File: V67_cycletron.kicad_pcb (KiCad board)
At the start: 4 copper layers, 101.9 x 49.8 mm, 33 parts, among them J1 USB_C_Receptacle_USB2.0_16P, J3 Screw_Terminal_01x11, U1 LM1117DT-5.0, U2 LM1117DT-3.3, U4 ESP32-S3-WROOM-1

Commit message: progress so far, believe I just need to ensure manufacture compatibility
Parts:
- removed vdo1: 5023520200, Connector_4:CONN_SD-502352-001_02_MOL
- added D1: D_Schottky, Diode_SMD:D_SMA, F.Cu at (79.8, 107.2)
- added Fan1: PC_Fan, connector_4_vert:CONN4_B4B-PH_JST, F.Cu at (137.5, 113.4)
- added HBridge1: B6B-PH-K-S, connector_6_vert:CONN_B6B-PH-K-S_JST, F.Cu at (101.5, 113.4)
- added HBridge2: B2B-PH-K-S, connector_2_vert:CONN2_B2B-PH-K-S_JST, F.Cu at (119.3, 113.4)
- added Hall1: Hall_Sens, connector_3_vert:CONN_B3B-PH-K-SLFSN_JST, F.Cu at (126.8, 113.4)
- added I2C1: MCP9600, connector_4_vert:CONN4_B4B-PH_JST, F.Cu at (145.1, 107.9)
- added J2: Conn_01x04_Socket, Connector_PinHeader_1.27mm:PinHeader_1x04_P1.27mm_Vertical, F.Cu at (146.1, 93.3)
- added Mos1: B2B-PH-K-S, connector_2_vert:CONN2_B2B-PH-K-S_JST, F.Cu at (80.0, 114.3)
- added R3: 1k, Resistor_SMD:R_0805_2012Metric_Pad1.20x1.40mm_HandSolder, F.Cu at (107.7, 96.5)
- added R4: 4.7k, Resistor_SMD:R_0805_2012Metric_Pad1.20x1.40mm_HandSolder, F.Cu at (141.7, 107.2)
- added R5: 4.7k, Resistor_SMD:R_0805_2012Metric_Pad1.20x1.40mm_HandSolder, F.Cu at (141.7, 100.1)
- added Therm1: B2B-PH-K-S, connector_2_vert:CONN2_B2B-PH-K-S_JST, F.Cu at (92.1, 113.4)
- added mosfet4: HD2305, Package_TO_SOT_SMD:SOT-23, F.Cu at (84.8, 108.3)
- added tr3: 1k, Resistor_SMD:R_0805_2012Metric_Pad1.20x1.40mm_HandSolder, F.Cu at (85.4, 103.6)
- Input1: renamed from input1; value 5023520200 -> B2B-PH-K-S; footprint Connector_4:CONN_SD-502352-001_02_MOL -> connector_2_vert:CONN2_B2B-PH-K-S_JST
- J3: value Screw_Terminal_01x11 -> Conn_01x04_Socket; footprint TerminalBlock:TerminalBlock_MaiXu_MX126-5.0-11P_1x11_P5.00mm -> Connector_PinHeader_1.27mm:PinHeader_1x04_P1.27mm_Vertical
- Motor1: value 5023520400 -> Motor1; footprint Connector_4:CONN_SD-502352-001_04_MOL -> connector_4_vert:CONN4_B4B-PH_JST
- Motor2: value 5023520400 -> Motor2; footprint Connector_4:CONN_SD-502352-001_04_MOL -> connector_4_vert:CONN4_B4B-PH_JST
- moved Rails1 41.2 mm to (43.6, 76.8)
- moved C2 34.6 mm to (141.6, 81.0)
- moved C1 33.8 mm to (143.8, 81.0)
- moved R_En1 30.5 mm to (140.2, 85.0), turned to 90 degrees
- moved Boot1 29.6 mm to (144.8, 88.8)
- moved En1 29.6 mm to (144.8, 85.0), turned to 0 degrees
- moved J3 25.7 mm to (142.2, 93.2), turned to 0 degrees
- moved R_boot1 25.0 mm to (140.0, 89.2), turned to -90 degrees
- moved vd_c2 13.4 mm to (90.2, 107.3), turned to 180 degrees
- moved vd_c1 11.9 mm to (92.1, 104.1)
- moved Motor1 8.89 mm to (42.4, 113.2), turned to 90 degrees
- moved Motor2 6.64 mm to (42.4, 93.5), turned to 90 degrees
- moved Motor_1 5.30 mm to (73.9, 101.9)
- moved Motor_2 5.30 mm to (73.9, 85.6)
- moved vd_r1 4.97 mm to (97.2, 105.4), turned to 90 degrees
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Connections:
- J3 pad 1: I20 -> IO40
- J3 pad 2: I19 -> IO39
- J3 pad 3: I18 -> IO38
- J3 pad 4: I17 -> IO37
- Motor1 pad 1: Motor1_A1 -> Motor1_A2
- Motor1 pad 2: Motor1_A2 -> Motor1_A1
- Motor1 pad 3: Motor1_B2 -> Motor1_B1
- Motor1 pad 4: Motor1_B1 -> Motor1_B2
- Motor2 pad 3: Motor2_B2 -> Motor2_B1
- Motor2 pad 4: Motor2_B1 -> Motor2_B2
- U4 pad 10: I10 -> Motor2_DIR
- U4 pad 11: I11 -> Motor1_FLT
- U4 pad 12: I12 -> Motor1_EN
- U4 pad 15: I15 -> Motor1_M0
- U4 pad 16: I16 -> Motor1_M1
- U4 pad 17: I17 -> Motor1_M2
- U4 pad 18: I18 -> Motor1_STEP
- U4 pad 19: I19 -> Motor1_DIR
- U4 pad 20: I20 -> mosfet1_i
- U4 pad 22: mosfet1_i -> L_EN
- U4 pad 23: mosfet2_i -> R_EN
- U4 pad 24: mosfet3_i -> LPWM
- U4 pad 25: Motor1_FLT -> RPWM
- U4 pad 26: Motor1_EN -> Hall_i
- U4 pad 28: Motor1_M0 -> FAN_En_o
- U4 pad 29: Motor1_M1 -> FAN_Tach_i
- U4 pad 30: Motor1_M2 -> IO37
- U4 pad 31: Motor1_STEP -> IO38
- U4 pad 32: Motor1_DIR -> IO39
- U4 pad 33: Motor2_EN -> IO40
- U4 pad 34: Motor2_FLT -> SCL
- U4 pad 35: Motor2_M0 -> SDA
- U4 pad 36: Motor2_M1 -> RX
- U4 pad 37: Motor2_M2 -> TX
- U4 pad 38: Motor2_STEP -> IO2
- U4 pad 39: Motor2_DIR -> IO1
- U4 pad 4: IO4 -> Motor2_FLT
- U4 pad 5: IO5 -> Motor2_EN
- U4 pad 6: IO6 -> Motor2_M0
- U4 pad 7: IO7 -> Motor2_M1
- U4 pad 8: I08 -> Motor2_M2
- U4 pad 9: I09 -> Motor2_STEP
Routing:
- net Motor1_EN: track 0.00 -> 72.0 mm, vias 0 -> 1
- net Motor1_M0: track 0.00 -> 70.7 mm, vias 0 -> 1
- net Motor2_EN: track 0.00 -> 70.2 mm, vias 0 -> 1
- net Motor1_M1: track 0.00 -> 68.6 mm, vias 0 -> 1
- net Motor2_M0: track 0.00 -> 67.6 mm, vias 0 -> 1
- net Motor1_M2: track 0.00 -> 67.1 mm, vias 0 -> 1
- net Motor2_M1: track 0.00 -> 64.4 mm, vias 0 -> 1
- net Motor1_STEP: track 0.00 -> 61.7 mm, vias 0 -> 1
- net Motor2_M2: track 0.00 -> 59.8 mm, vias 0 -> 1
- net Motor1_DIR: track 0.00 -> 59.5 mm, vias 0 -> 1
- net Motor2_STEP: track 0.00 -> 52.7 mm, vias 0 -> 1
- net Motor1_FLT: track 0.00 -> 52.1 mm, vias 0 -> 1
- net Motor2_DIR: track 0.00 -> 49.5 mm, vias 0 -> 1
- net Motor2_FLT: track 0.00 -> 49.1 mm, vias 0 -> 1
- net mosfet1_i: track 0.00 -> 44.4 mm
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- added copper zone on F.Cu, net +12V
- added copper zone on In1.Cu, net 3V3
- added copper zone on In2.Cu, net GND
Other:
- board size 101.9 x 49.8 mm -> 107.8 x 44.1 mm
- board text added: "0.01uF"
- board text added: "100"
- board text added: "100nF"
- board text added: "100uF"
- board text added: "10uF"
- board text added: "1k"
- board text added: "1uF"
- board text added: "2.2uF"
- board text added: "22uF"
- board text added: "3v3"
- board text added: "4.7k"
- board text added: "5.1k"
- board text added: "A1"
- board text added: "A2"
- board text added: "B1"
- board text added: "B2"
- board text added: "EN"
- board text added: "GND"
- board text added: "Hall"
- board text added: "In"
- board text added: "Input"
- board text added: "LEN"
- board text added: "LP"
- board text added: "REN"
- board text added: "RP"
- board text added: "SCL"
- board text added: "SDA"
- board text added: "Tach"

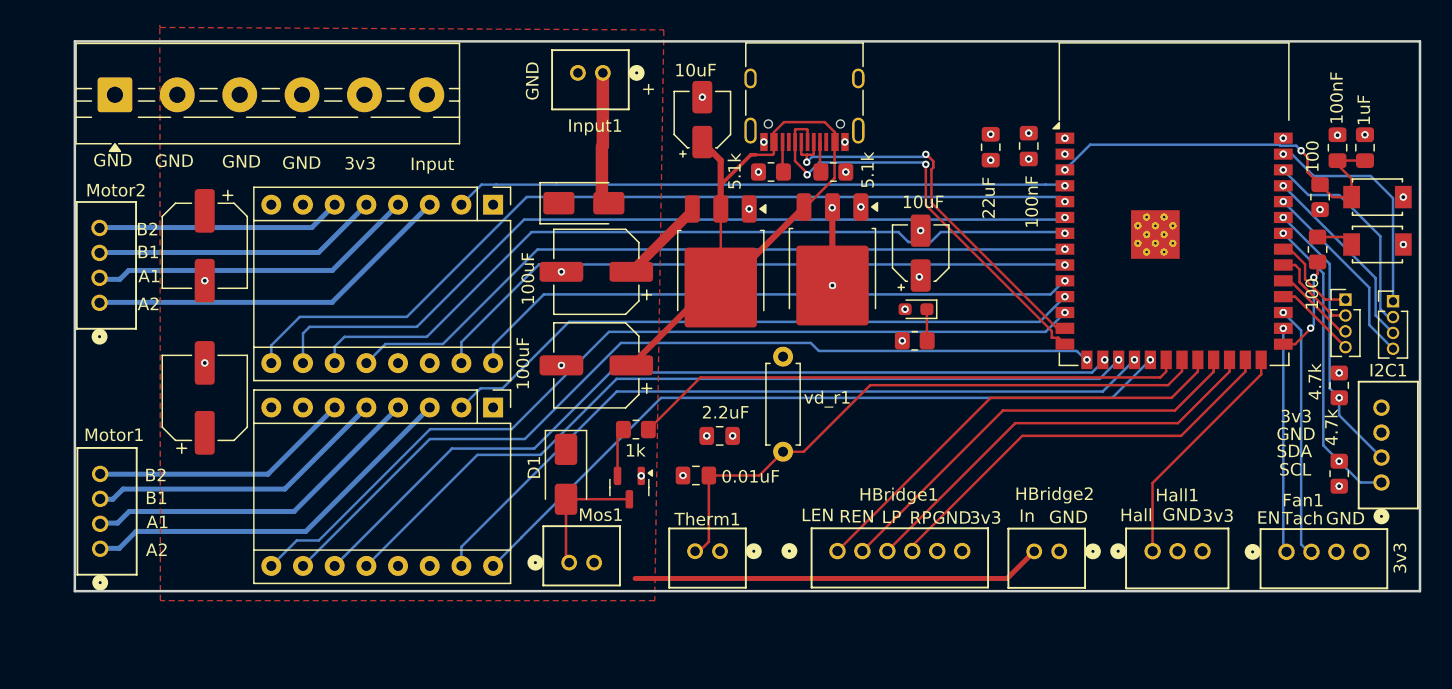
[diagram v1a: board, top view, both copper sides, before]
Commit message: re-arranged connector positions
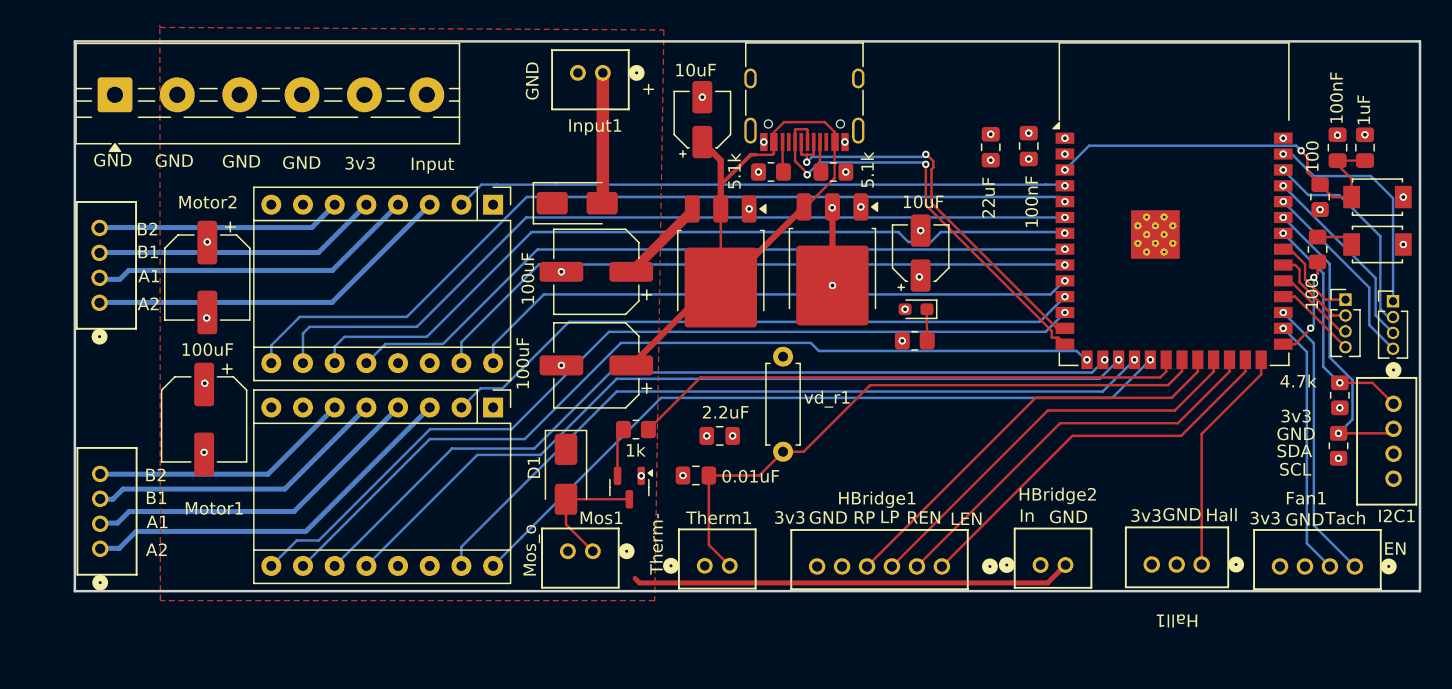
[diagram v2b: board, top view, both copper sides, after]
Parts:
- moved HBridge1 8.46 mm to (109.9, 114.6), turned to 180 degrees
- moved I2C1 6.38 mm to (146.1, 101.6), turned to -90 degrees
- moved R4 6.28 mm to (141.8, 100.9)
- moved Fan1 5.60 mm to (143.0, 114.6), turned to 180 degrees
- moved R5 4.85 mm to (141.7, 104.9), turned to 90 degrees
- moved Hall1 4.07 mm to (130.7, 114.5), turned to 0 degrees
- moved motorc2 2.55 mm to (51.0, 91.4)
- moved Mos1 2.11 mm to (81.9, 113.4), turned to 0 degrees
- moved HBridge2 1.85 mm to (117.8, 114.5), turned to 180 degrees
- moved motorc1 1.73 mm to (50.7, 102.8), turned to -90 degrees
- moved Therm1 1.69 mm to (90.9, 114.6), turned to 180 degrees
- moved Dpower1 0.53 mm to (80.7, 85.5)
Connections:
- Fan1 pad 1: FAN_En_o -> FAN_Tach_i
- Fan1 pad 2: FAN_Tach_i -> FAN_En_o
- U4 pad 22: L_EN -> RPWM
- U4 pad 23: R_EN -> LPWM
- U4 pad 24: LPWM -> R_EN
- U4 pad 25: RPWM -> L_EN
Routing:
- net SCL: track 24.2 -> 18.9 mm
- net L_EN: track 35.8 -> 31.8 mm
- net R_EN: track 35.1 -> 32.5 mm
- net FAN_En_o: track 18.3 -> 20.6 mm
- net FAN_Tach_i: track 20.4 -> 22.7 mm
- net +12V: track 42.2 -> 44.4 mm, vias 0 -> 2
- net SDA: track 22.5 -> 24.6 mm
- net Therm-: track 49.2 -> 50.3 mm
- net LPWM: track 34.3 -> 33.2 mm
- net Hall_i: track 19.2 -> 18.4 mm
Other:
- board text added: "Mos_o"
- board text added: "Therm-"

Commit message: idk changes
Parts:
- moved R2 6.49 mm to (107.7, 83.4)
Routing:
- net +5V: track 53.0 -> 46.8 mm
- net Net-(J1-CC1): track 2.64 -> 8.35 mm, vias 0 -> 2
- net D+: track 35.3 -> 32.3 mm, vias 2 -> 0
- net D-: track 32.4 -> 31.8 mm, vias 2 -> 0
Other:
- board text added: "Dev: Ryan Taylor"

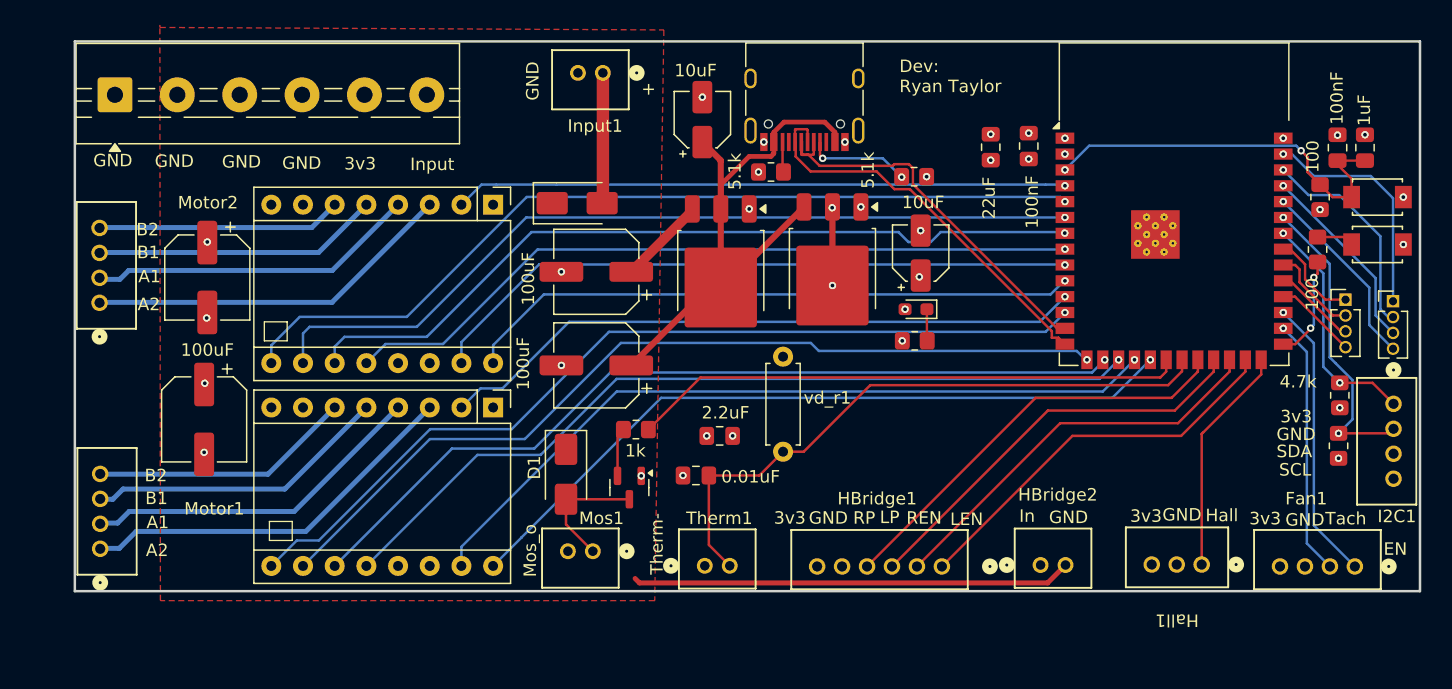
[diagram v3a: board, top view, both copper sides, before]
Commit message: edits to part selection, new regulator
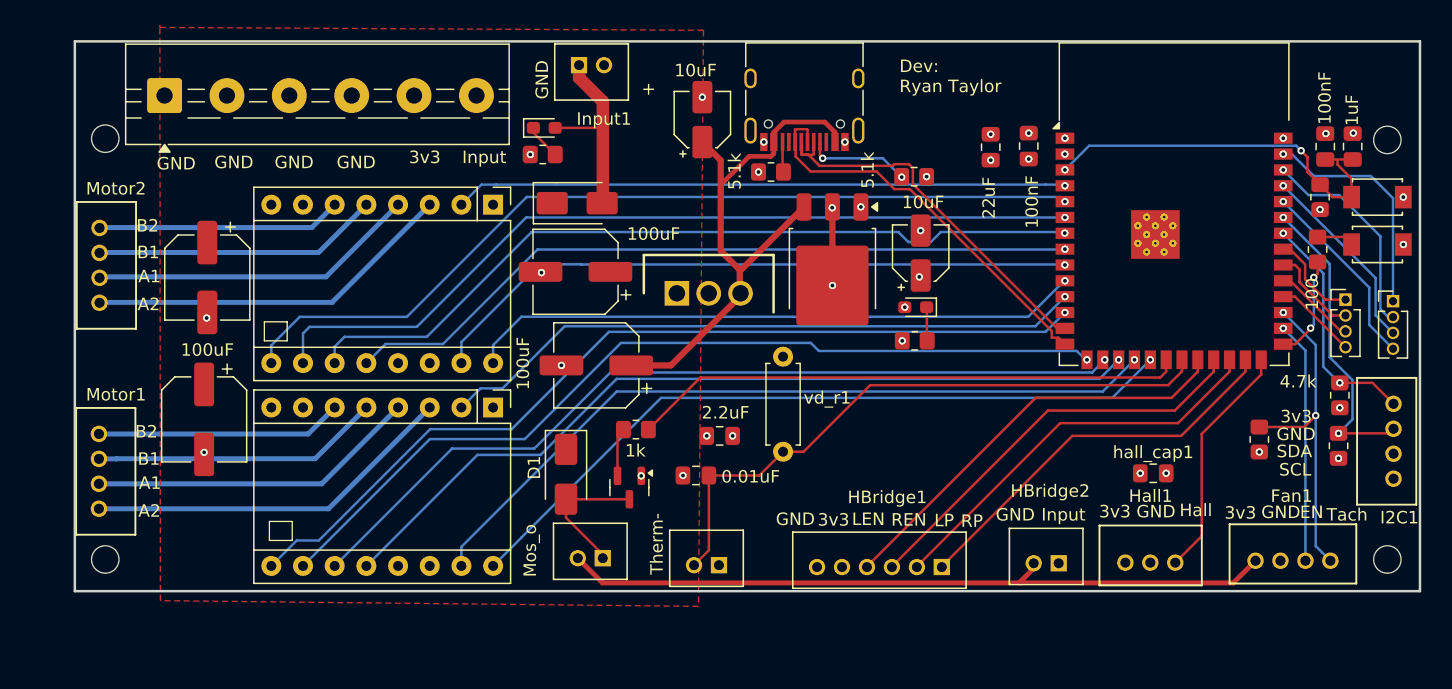
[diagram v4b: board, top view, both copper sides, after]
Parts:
- removed U1: LM1117DT-5.0, Package_TO_SOT_SMD:TO-252-3_TabPin2
- added ?: , , F.Cu at (145.6, 114.0)
- added ?: , , F.Cu at (42.8, 80.3)
- added ?: , , F.Cu at (145.6, 80.4)
- added ?: , , F.Cu at (42.8, 114.0)
- added D5: LED, LED_SMD:LED_0603_1608Metric_Pad1.05x0.95mm_HandSolder, F.Cu at (78.0, 79.5)
- added R6: 1k, Resistor_SMD:R_0805_2012Metric_Pad1.20x1.40mm_HandSolder, F.Cu at (77.9, 81.6)
- added R7: 4.7k, Resistor_SMD:R_0805_2012Metric_Pad1.20x1.40mm_HandSolder, F.Cu at (135.3, 104.4)
- added U3: L7805, regulator_5V:TO255P460X1020X2008-3P, F.Cu at (88.6, 92.7)
- added hall_cap1: 100nF, Capacitor_SMD:C_0805_2012Metric_Pad1.18x1.45mm_HandSolder, F.Cu at (126.8, 107.1)
- HBridge1: footprint connector_6_vert:CONN_B6B-PH-K-S_JST -> connector_6_vert:JST_B6B-PH-K-S
- HBridge2, Input1, Mos1, Therm1: footprint connector_2_vert:CONN2_B2B-PH-K-S_JST -> connector_2_vert:JST_B2B-PH-K-S
- vd_r1: value 4.6k -> 4.7k
- moved HBridge1 5.03 mm to (104.9, 114.1), turned to 0 degrees
- moved Rails1 3.98 mm to (47.6, 76.9)
- moved Motor1 3.21 mm to (42.3, 110.0)
- moved Hall1 2.12 mm to (128.6, 114.3)
- moved Fan1 2.01 mm to (141.0, 114.1)
- moved 5Vin1 1.67 mm to (80.5, 91.0)
- moved C1 0.99 mm to (142.8, 80.9)
- moved C2 0.99 mm to (140.6, 80.9)
- moved Input1 0.91 mm to (81.8, 75.0), turned to 180 degrees
- moved HBridge2 0.82 mm to (118.2, 113.8), turned to 0 degrees
- moved Therm1 0.62 mm to (91.0, 114.0), turned to 0 degrees
- moved Mos1 0.21 mm to (81.7, 113.4)
- moved D4 0.16 mm to (107.8, 93.8)
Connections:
- net Net-(Dpower1-A) renamed 24V_unsafe
- 5Vin1 pad 1: +12V -> +24V
- D1 pad 1: +12V -> +24V
- Dpower1 pad 1: +12V -> +24V
- Fan1 pad 4: 3V3 -> +24V
- HBridge1 pad 1: L_EN -> RPWM
- HBridge1 pad 2: R_EN -> LPWM
- HBridge1 pad 3: LPWM -> R_EN
- HBridge1 pad 4: RPWM -> L_EN
- HBridge1 pad 5: GND -> 3V3
- HBridge1 pad 6: 3V3 -> GND
- HBridge2 pad 2: +12V -> +24V
- Mos1 pad 2: +12V -> +24V
- Motor_1 pad 8: +12V -> +24V
- Motor_2 pad 8: +12V -> +24V
- Rails1 pad 6: +12V -> +24V
- U4 pad 22: RPWM -> L_EN
- U4 pad 23: LPWM -> R_EN
- U4 pad 24: R_EN -> LPWM
- U4 pad 25: L_EN -> RPWM
- motorc1 pad 1: +12V -> +24V
- motorc2 pad 1: +12V -> +24V
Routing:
- net +24V: track 0.00 -> 60.0 mm
- net +12V: track 44.4 -> 0.00 mm, vias 2 -> 0
- net 24V_unsafe: track 11.0 -> 16.4 mm
- net FAN_Tach_i: track 22.7 -> 26.4 mm, vias 1 -> 2
- net Net-(D5-K): track 0.00 -> 2.86 mm
- net RPWM: track 33.9 -> 31.8 mm
- net L_EN: track 31.8 -> 33.9 mm
- net FAN_En_o: track 20.6 -> 19.4 mm
- net Motor1_A1: track 27.8 -> 26.5 mm
- net Motor1_A2: track 31.1 -> 29.9 mm
- net Motor1_B2: track 21.0 -> 19.8 mm
- net Motor1_B1: track 24.4 -> 23.3 mm
- net mosfet1_o: track 10.6 -> 11.5 mm
- net R_EN: track 32.5 -> 33.2 mm
- net LPWM: track 33.2 -> 32.5 mm
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- added copper zone on F.Cu, net +24V
- removed copper zone on F.Cu, net +12V
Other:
- board text removed: "In"
